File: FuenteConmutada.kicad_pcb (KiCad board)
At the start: 2 copper layers, 9 parts, among them J2 Conn_01x02_Socket, P1 USB_C_Plug_USB2.0, U1 MT3608

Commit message: avance en ruteo
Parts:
- moved J2 33.0 mm to (108.6, 73.0)
- moved C2 24.5 mm to (105.4, 74.0), turned to 90 degrees
- moved D1 21.9 mm to (99.1, 68.5), turned to 90 degrees
- moved P1 20.8 mm to (80.6, 69.2), turned to -90 degrees
- moved R1 19.6 mm to (88.3, 73.6), turned to -90 degrees
- moved L1 17.2 mm to (108.0, 65.7), turned to 90 degrees
- moved U1 14.7 mm to (92.2, 72.7)
- moved C1 12.7 mm to (93.0, 75.9)
- moved RV1 10.2 mm to (90.2, 62.9), turned to 90 degrees
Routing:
- net Net-(U1-EN): track 0.00 -> 33.3 mm
- net GND: track 0.00 -> 29.6 mm
- net Net-(J2-Pin_1): track 0.00 -> 3.46 mm
- net Net-(U1-SW): track 0.00 -> 1.04 mm
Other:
- board outline added: 36.2 x 17.8 mm

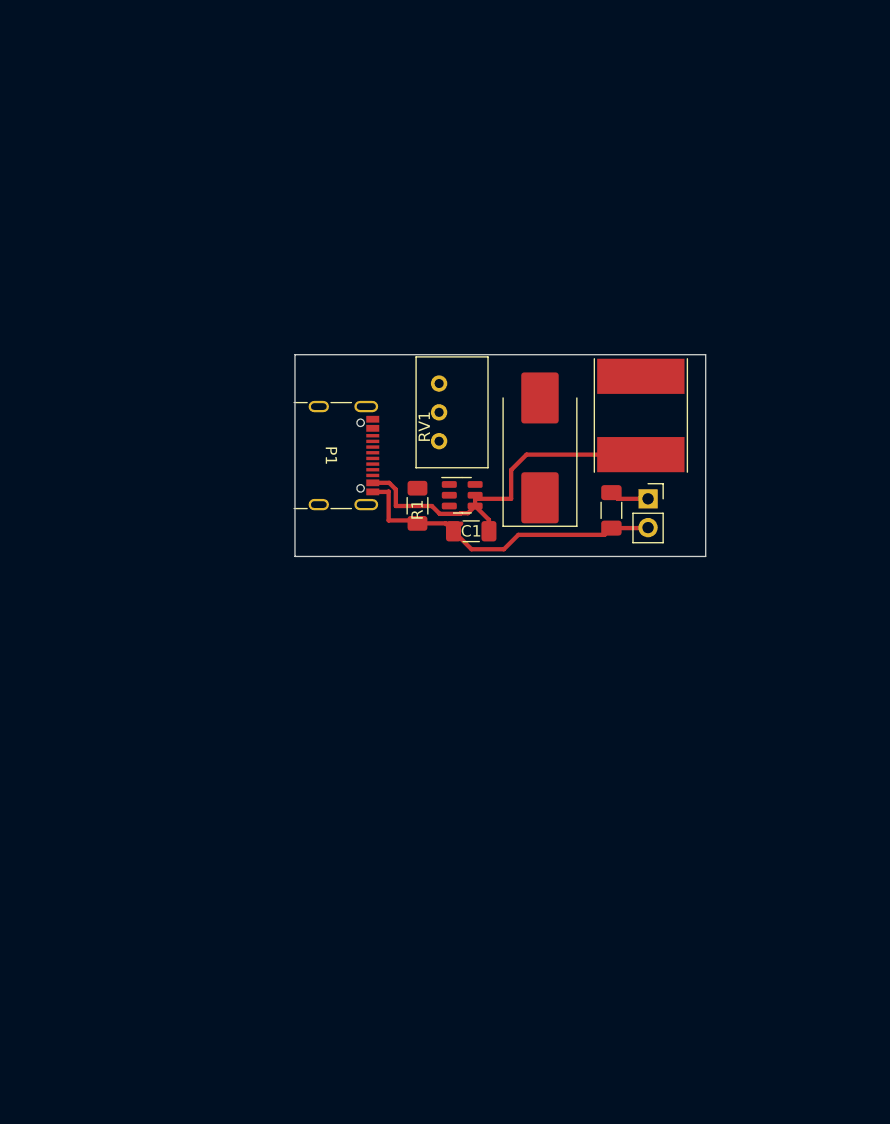
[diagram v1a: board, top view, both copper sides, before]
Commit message: Esquematico 3in1 + Simbolo LMR64010 + Simu LT1930
Esquematico placa de prueba Boost-SEPIC-Fuente partida;
Simbolo para simulacion de LMR64010(xxx.asy debe estar en la misma carpeta);
Simulacion pasos del potenciometro, permite seleccionar el valor del pote(depende del valor de R2, L, RL)
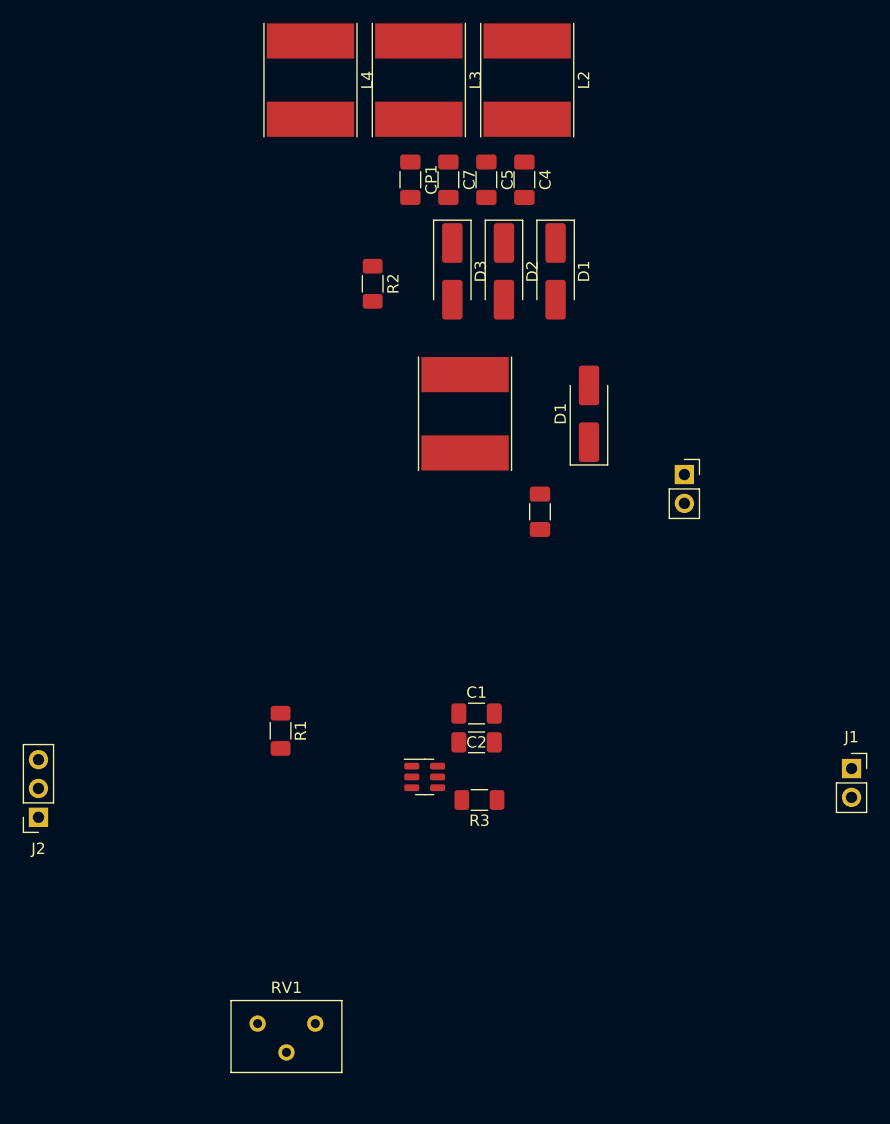
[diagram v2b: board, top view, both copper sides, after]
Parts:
- removed the D1 at (99.1, 68.5)
- removed P1: USB_C_Plug_USB2.0, Connector_USB:USB_C_Receptacle_GCT_USB4105-xx-A_16P_TopMnt_Horizontal
- added C1: 22uF, Capacitor_SMD:C_1206_3216Metric_Pad1.33x1.80mm_HandSolder, F.Cu at (93.5, 91.9)
- added C4: 22uF, Capacitor_SMD:C_1206_3216Metric_Pad1.33x1.80mm_HandSolder, F.Cu at (97.7, 44.9)
- added C5: 1uF, Capacitor_SMD:C_1206_3216Metric_Pad1.33x1.80mm_HandSolder, F.Cu at (94.3, 44.9)
- added C7: 22uF, Capacitor_SMD:C_1206_3216Metric_Pad1.33x1.80mm_HandSolder, F.Cu at (91.0, 44.9)
- added CP1: 1uF, Capacitor_SMD:C_1206_3216Metric_Pad1.33x1.80mm_HandSolder, F.Cu at (87.6, 44.9)
- added D1: D_Schottky, Diode_SMD:D_SMA_Handsoldering, F.Cu at (100.4, 53.0)
- added D1: D_Schottky, Diode_SMD:D_SMA_Handsoldering, F.Cu at (103.4, 65.5)
- added D2: D_Schottky, Diode_SMD:D_SMA_Handsoldering, F.Cu at (95.9, 53.0)
- added D3: D_Schottky, Diode_SMD:D_SMA_Handsoldering, F.Cu at (91.3, 53.0)
- added J1: Conn_01x02_Socket, Connector_PinSocket_2.54mm:PinSocket_1x02_P2.54mm_Vertical, F.Cu at (126.5, 96.8)
- added J2: Conn_01x03_Socket, Connector_PinSocket_2.54mm:PinSocket_1x03_P2.54mm_Vertical, F.Cu at (54.9, 101.1)
- added L2: 10uH, Inductor_SMD:L_Taiyo-Yuden_NR-80xx_HandSoldering, F.Cu at (97.9, 36.1)
- added L3: 10uH, Inductor_SMD:L_Taiyo-Yuden_NR-80xx_HandSoldering, F.Cu at (88.4, 36.1)
- added L4: 10uH, Inductor_SMD:L_Taiyo-Yuden_NR-80xx_HandSoldering, F.Cu at (78.8, 36.1)
- added R2: R, Resistor_SMD:R_1206_3216Metric_Pad1.30x1.75mm_HandSolder, F.Cu at (84.3, 54.1)
- added R3: R, Resistor_SMD:R_1206_3216Metric_Pad1.30x1.75mm_HandSolder, F.Cu at (93.7, 99.6)
- RV1: footprint Potentiometer_THT:Potentiometer_Bourns_3299W_Vertical -> Potentiometer_THT:Potentiometer_Bourns_3299Y_Vertical
- moved RV1 57.5 mm to (79.3, 119.3), turned to 0 degrees
- moved U1 25.0 mm to (88.9, 97.5)
- moved R1 23.2 mm to (76.2, 93.5), turned to 90 degrees
- moved C2 18.6 mm to (93.5, 94.5)
- moved L1 15.5 mm to (92.5, 65.5)
- moved C3 6.30 mm to (99.1, 74.2)
- moved J2 3.85 mm to (111.8, 70.9)
- renumbered C1 to C2, C2 to C3
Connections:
- C2 pad 2: Net-(U1-EN) -> Net-(J1-Pin_1)
- C3 pad 2: Net-(J2-Pin_1) -> Net-(D1-K)
- J2 pad 1: Net-(J2-Pin_1) -> Net-(D1-K)
- L1 pad 1: Net-(U1-EN) -> Net-(J1-Pin_1)
- L1 pad 2: Net-(U1-SW) -> Net-(L1-Pad2)
- R1 pad 1: Net-(R1-Pad1) -> Net-(U1-FB)
- RV1 pad 1: Net-(U1-SW) -> Net-(D1-K)
- RV1 pad 3: Net-(R1-Pad1) -> Net-(U1-FB)
- U1 pad 5: Net-(U1-EN) -> Net-(J1-Pin_1)
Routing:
- net Net-(U1-EN): track 33.3 -> 0.00 mm
- net GND: track 29.6 -> 0.00 mm
- net Net-(J2-Pin_1): track 3.46 -> 0.00 mm
- net Net-(U1-SW): track 1.04 -> 0.00 mm
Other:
- board outline removed

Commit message: PCB
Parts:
- removed the D1 at (100.4, 53.0)
- removed the D1 at (103.4, 65.5)
- removed the J2 at (111.8, 70.9)
- added D1: D_Schottky, Diode_SMD:D_SMA_Handsoldering, F.Cu at (82.0, 84.3)
- moved L3 64.0 mm to (71.4, 97.8), turned to 0 degrees
- moved C4 59.0 mm to (78.2, 100.6)
- moved L4 56.7 mm to (82.0, 92.7), turned to 0 degrees
- moved C7 49.8 mm to (90.7, 94.7), turned to 90 degrees
- moved L2 49.8 mm to (108.5, 84.8), turned to 180 degrees
- moved CP1 40.0 mm to (95.5, 84.1)
- moved C5 39.8 mm to (88.6, 84.3)
- moved D3 37.0 mm to (93.0, 89.9), turned to 180 degrees
- moved D2 32.7 mm to (100.3, 85.3), turned to 90 degrees
- moved L1 32.4 mm to (108.5, 93.7), turned to 0 degrees
- moved C3 31.8 mm to (81.3, 100.6), turned to -90 degrees
- moved R2 31.1 mm to (91.4, 84.3)
- moved RV1 22.3 mm to (93.0, 101.7)
- moved J2 20.5 mm to (71.1, 88.6)
- moved J1 18.8 mm to (108.2, 101.1)
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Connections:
- net Net-(D1-K) renamed /Vo+
- net Net-(D3-A) renamed /Vo-
- net Net-(J1-Pin_1) renamed /Vin
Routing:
- net /Vo+: track 0.00 -> 70.4 mm
- net GND: track 0.00 -> 69.6 mm
- net /Vo-: track 0.00 -> 25.4 mm
- net /Vin: track 0.00 -> 23.4 mm
- net Net-(U1-SW): track 0.00 -> 21.2 mm
- net Net-(L2-Pad2): track 0.00 -> 18.7 mm
- net Net-(U1-FB): track 0.00 -> 15.5 mm
- net Net-(D2-A): track 0.00 -> 10.5 mm
- net Net-(L1-Pad2): track 0.00 -> 8.89 mm
- net Net-(L3-Pad2): track 0.00 -> 7.95 mm
- net Net-(D1-A): track 0.00 -> 4.75 mm
- net Net-(U1-EN): track 0.00 -> 2.59 mm

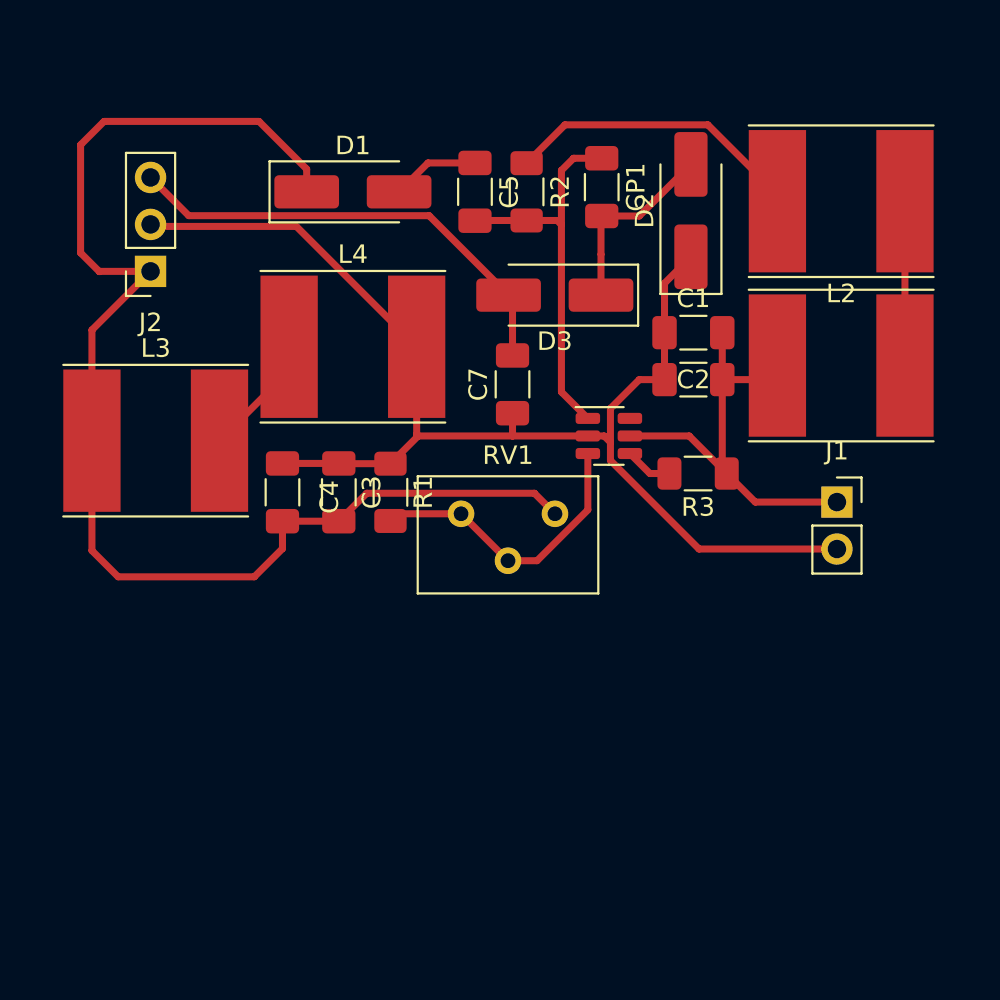
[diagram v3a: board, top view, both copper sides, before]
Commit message: pote y  área
Cambios en huella de pote multi , 3 pines alineados y agregado del área de 5cm x 5cm
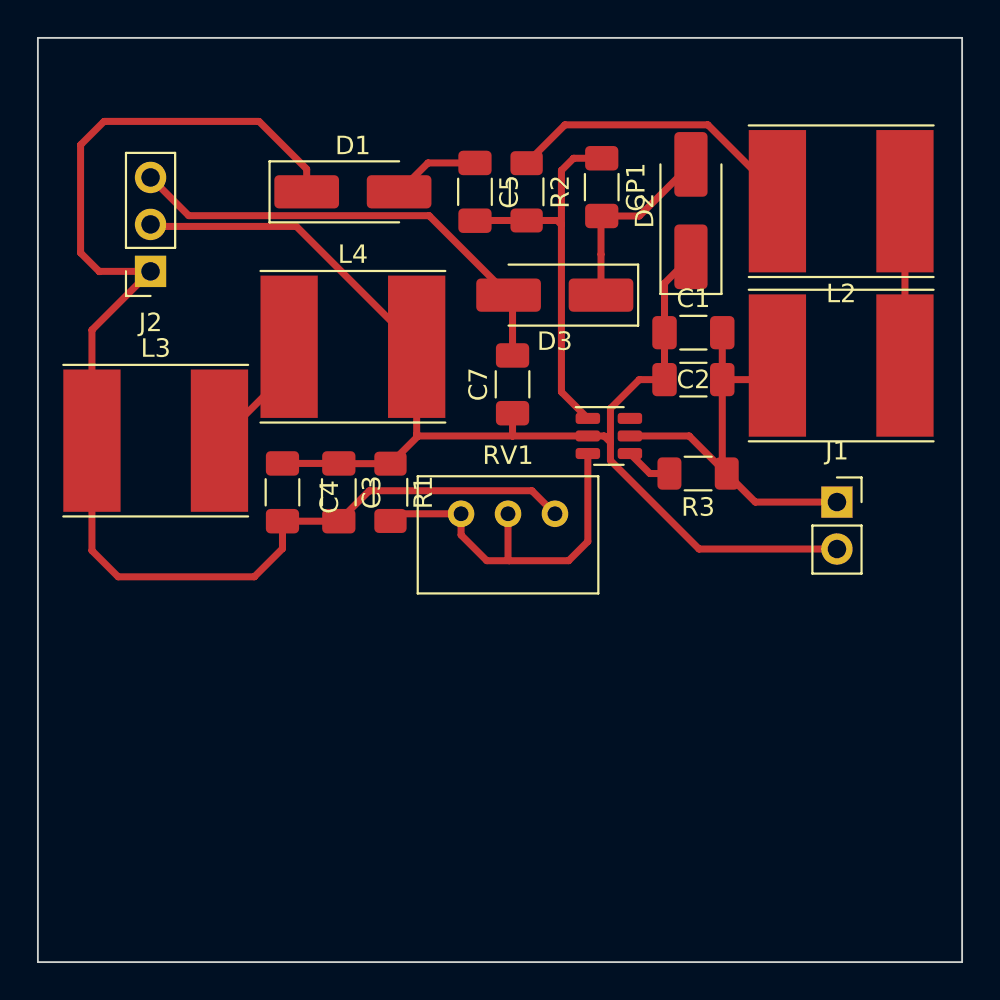
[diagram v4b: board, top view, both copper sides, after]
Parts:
- RV1: footprint Potentiometer_THT:Potentiometer_Bourns_3299Y_Vertical -> Potentiometer_THT:Potentiometer_Bourns_3299W_Vertical
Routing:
- net Net-(U1-FB): track 15.5 -> 19.8 mm
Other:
- board outline added: 50 x 50 mm
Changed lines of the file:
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@@
     )
   )
-  (footprint "Potentiometer_THT:Potentiometer_Bourns_3299Y_Vertical" (layer "F.Cu")
+  (footprint "Potentiometer_THT:Potentiometer_Bourns_3299W_Vertical" (layer "F.Cu")
     (at 92.974 101.745)
-    (descr "Potentiometer, vertical, Bourns 3299Y, https://www.bourns.com/pdfs/3299.pdf")
-    (tags "Potentiometer vertical Bourns 3299Y")
+    (descr "Potentiometer, vertical, Bourns 3299W, https://www.bourns.com/pdfs/3299.pdf")
+    (tags "Potentiometer vertical Bourns 3299W")
     (property "Sheetfile" "FuenteConmutada.kicad_sch")
     (property "Sheetname" "")
@@
     (pad "1" thru_hole circle (at 0 0) (size 1.44 1.44) (drill 0.8) (layers "*.Cu" "*.Mask")
       (net 5 "/Vo+") (pinfunction "1") (pintype "passive"))
-    (pad "2" thru_hole circle (at -2.54 2.54) (size 1.44 1.44) (drill 0.8) (layers "*.Cu" "*.Mask")
+    (pad "2" thru_hole circle (at -2.54 0) (size 1.44 1.44) (drill 0.8) (layers "*.Cu" "*.Mask")
       (net 6 "Net-(U1-FB)") (pinfunction "2") (pintype "passive"))
     (pad "3" thru_hole circle (at -5.08 0) (size 1.44 1.44) (drill 0.8) (layers "*.Cu" "*.Mask")
       (net 6 "Net-(U1-FB)") (pinfunction "3") (pintype "passive"))
-    (model "${KICAD6_3DMODEL_DIR}/Potentiometer_THT.3dshapes/Potentiometer_Bourns_3299Y_Vertical.wrl"
+    (model "${KICAD6_3DMODEL_DIR}/Potentiometer_THT.3dshapes/Potentiometer_Bourns_3299W_Vertical.wrl"
       (offset (xyz 0 0 0))
       (scale (xyz 1 1 1))
@@
     )
   )
+  (gr_rect (start 65 76) (end 115 126)
+    (stroke (width 0.1) (type default)) (fill none) (layer "Edge.Cuts"))
   (segment (start 98.9 91.948) (end 98.9 94.488) (width 0.381) (layer "F.Cu") (net 1))
   (segment (start 90.678 97.536) (end 85.572 97.536) (width 0.381) (layer "F.Cu") (net 1))
@@
   (segment (start 103.8105 101.112) (end 102.2665 99.568) (width 0.381) (layer "F.Cu") (net 4))
   (segment (start 79.542 83.098) (end 76.962 80.518) (width 0.381) (layer "F.Cu") (net 5))
-  (segment (start 82.792 100.6345) (end 91.8635 100.6345) (width 0.381) (layer "F.Cu") (net 5))
   (segment (start 67.924 103.738) (end 67.924 97.79) (width 0.381) (layer "F.Cu") (net 5))
   (segment (start 78.232 102.1465) (end 78.232 103.632) (width 0.381) (layer "F.Cu") (net 5))
@@
   (segment (start 79.542 84.328) (end 79.542 83.098) (width 0.381) (layer "F.Cu") (net 5))
   (segment (start 76.708 105.156) (end 69.342 105.156) (width 0.381) (layer "F.Cu") (net 5))
-  (segment (start 81.28 102.1465) (end 82.792 100.6345) (width 0.381) (layer "F.Cu") (net 5))
+  (segment (start 81.28 102.1465) (end 82.9265 100.5) (width 0.381) (layer "F.Cu") (net 5))
+  (segment (start 82.9265 100.5) (end 91.729 100.5) (width 0.381) (layer "F.Cu") (net 5))
   (segment (start 69.342 105.156) (end 67.924 103.738) (width 0.381) (layer "F.Cu") (net 5))
+  (segment (start 91.729 100.5) (end 92.974 101.745) (width 0.381) (layer "F.Cu") (net 5))
   (segment (start 67.924 97.79) (end 67.924 91.802) (width 0.381) (layer "F.Cu") (net 5))
   (segment (start 76.962 80.518) (end 68.58 80.518) (width 0.381) (layer "F.Cu") (net 5))
@@
   (segment (start 67.31 81.788) (end 67.31 87.63) (width 0.381) (layer "F.Cu") (net 5))
   (segment (start 67.31 87.63) (end 68.326 88.646) (width 0.381) (layer "F.Cu") (net 5))
-  (segment (start 91.8635 100.6345) (end 92.974 101.745) (width 0.381) (layer "F.Cu") (net 5))
   (segment (start 81.28 102.1465) (end 78.232 102.1465) (width 0.381) (layer "F.Cu") (net 5))
   (segment (start 67.924 91.802) (end 71.095 88.631) (width 0.381) (layer "F.Cu") (net 5))
   (segment (start 78.232 103.632) (end 76.708 105.156) (width 0.381) (layer "F.Cu") (net 5))
-  (segment (start 94.753 98.486) (end 94.753 101.536485) (width 0.381) (layer "F.Cu") (net 6))
-  (segment (start 87.894 101.745) (end 90.434 104.285) (width 0.381) (layer "F.Cu") (net 6))
-  (segment (start 94.753 101.536485) (end 92.004485 104.285) (width 0.381) (layer "F.Cu") (net 6))
+  (segment (start 90.434 104.219) (end 90.5 104.285) (width 0.381) (layer "F.Cu") (net 6))
+  (segment (start 93.715 104.285) (end 90.5 104.285) (width 0.381) (layer "F.Cu") (net 6))
+  (segment (start 90.5 104.285) (end 89.285 104.285) (width 0.381) (layer "F.Cu") (net 6))
+  (segment (start 94.753 103.247) (end 93.715 104.285) (width 0.381) (layer "F.Cu") (net 6))
+  (segment (start 94.753 98.486) (end 94.753 103.247) (width 0.381) (layer "F.Cu") (net 6))
+  (segment (start 90.434 101.745) (end 90.434 104.219) (width 0.381) (layer "F.Cu") (net 6))
+  (segment (start 87.894 102.894) (end 87.894 101.745) (width 0.381) (layer "F.Cu") (net 6))
+  (segment (start 89.285 104.285) (end 87.894 102.894) (width 0.381) (layer "F.Cu") (net 6))
   (segment (start 87.894 101.745) (end 84.463 101.745) (width 0.381) (layer "F.Cu") (net 6))
-  (segment (start 92.004485 104.285) (end 90.434 104.285) (width 0.381) (layer "F.Cu") (net 6))
   (segment (start 91.44 85.878) (end 93.0955 85.878) (width 0.381) (layer "F.Cu") (net 8))
   (segment (start 94.753 96.586) (end 93.3235 95.1565) (width 0.381) (layer "F.Cu") (net 8))
